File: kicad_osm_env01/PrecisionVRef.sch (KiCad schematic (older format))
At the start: 12 parts

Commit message: schematics awaiting review
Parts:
- added TP86: Test_Point, TestPoint:TestPoint_THTPad_D1.0mm_Drill0.5mm, symbol OSM_env01-rescue:Test_Point-Connector-ESP32-EVB_Rev_D-rescue
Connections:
- net 3V3_AN: now also TP86.1
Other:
- moved on the sheet: C63, C64, C65, L3
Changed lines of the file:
@@
 AR Path="/608F4675/61105411/611114A1" Ref="TP?"  Part="1"
 AR Path="/61323885/611114A1" Ref="TP58"  Part="1"
-F 0 "TP58" V 6320 3797 50  0000 C CNN
-F 1 "Test_Point" V 6229 3797 50  0000 C CNN
+F 0 "TP58" V 6125 4000 50  0000 C CNN
+F 1 "Test_Point" V 6229 3797 50  0001 C CNN
 F 2 "" H 6325 3725 50  0001 C CNN
 F 3 "~" H 6325 3725 50  0001 C CNN
@@
 L power:+5V #PWR?
 U 1 1 611114A7
-P 3275 3525
+P 2725 3550
 AR Path="/608F4675/60959880/611114A7" Ref="#PWR?"  Part="1"
 AR Path="/608F4675/61105411/611114A7" Ref="#PWR?"  Part="1"
 AR Path="/61323885/611114A7" Ref="#PWR0124"  Part="1"
-F 0 "#PWR0124" H 3275 3375 50  0001 C CNN
-F 1 "+5V" H 3290 3698 50  0000 C CNN
-F 2 "" H 3275 3525 50  0001 C CNN
-F 3 "" H 3275 3525 50  0001 C CNN
-	1    3275 3525
+F 0 "#PWR0124" H 2725 3400 50  0001 C CNN
+F 1 "+5V" H 2740 3723 50  0000 C CNN
+F 2 "" H 2725 3550 50  0001 C CNN
+F 3 "" H 2725 3550 50  0001 C CNN
+	1    2725 3550
 	1    0    0    -1
 $EndComp
@@
 L device:Ferrite_Bead L?
 U 1 1 611114BF
-P 3700 3800
+P 3150 3825
 AR Path="/608F4675/60959880/611114BF" Ref="L?"  Part="1"
 AR Path="/608F4675/61105411/611114BF" Ref="L?"  Part="1"
 AR Path="/61323885/611114BF" Ref="L3"  Part="1"
-F 0 "L3" V 3426 3800 50  0000 C CNN
-F 1 "Ferrite_Bead" V 3517 3800 50  0000 C CNN
-F 2 "" V 3630 3800 50  0001 C CNN
-F 3 "" H 3700 3800 50  0001 C CNN
-	1    3700 3800
+F 0 "L3" V 2876 3825 50  0000 C CNN
+F 1 "Ferrite_Bead" V 2967 3825 50  0000 C CNN
+F 2 "" V 3080 3825 50  0001 C CNN
+F 3 "" H 3150 3825 50  0001 C CNN
+	1    3150 3825
 	0    -1   1    0
 $EndComp
@@
 L device:C C?
 U 1 1 611114C5
-P 4650 3950
+P 4100 3975
 AR Path="/608F4675/60959880/611114C5" Ref="C?"  Part="1"
 AR Path="/608F4675/61105411/611114C5" Ref="C?"  Part="1"
 AR Path="/61323885/611114C5" Ref="C64"  Part="1"
-F 0 "C64" H 4765 3996 50  0000 L CNN
-F 1 "10nF" H 4765 3905 50  0000 L CNN
-F 2 "" H 4688 3800 50  0001 C CNN
-F 3 "" H 4650 3950 50  0001 C CNN
-	1    4650 3950
-	-1   0    0    -1
-$EndComp
-Wire Wire Line
-	3550 3800 3275 3800
-Wire Wire Line
-	3275 3525 3275 3800
-Wire Wire Line
-	5125 4200 5125 4100
-Text Label 5450 3800 2    50   ~ 0
+F 0 "C64" H 4215 4021 50  0000 L CNN
+F 1 "10nF" H 4215 3930 50  0000 L CNN
+F 2 "" H 4138 3825 50  0001 C CNN
+F 3 "" H 4100 3975 50  0001 C CNN
+	1    4100 3975
+	-1   0    0    -1
+$EndComp
+Wire Wire Line
+	3000 3825 2725 3825
+Wire Wire Line
+	2725 3550 2725 3825
+Wire Wire Line
+	4575 4225 4575 4125
+Text Label 4900 3825 2    50   ~ 0
 5V_AN
 Wire Wire Line
@@
 $EndComp
 Wire Wire Line
-	8600 3725 8925 3725
+	8600 3725 8750 3725
 Wire Wire Line
 	6625 3725 6975 3725
@@
 Wire Wire Line
 	7275 3725 7675 3725
-Text HLabel 5450 3800 2    50   Input ~ 0
+Text HLabel 4900 3825 2    50   Input ~ 0
 5V_AN
 Text HLabel 8925 3725 2    50   Input ~ 0
@@
 L device:C C?
 U 1 1 61203E74
-P 5125 3950
+P 4575 3975
 AR Path="/608F4675/60959880/61203E74" Ref="C?"  Part="1"
 AR Path="/608F4675/61105411/61203E74" Ref="C?"  Part="1"
 AR Path="/61323885/61203E74" Ref="C65"  Part="1"
-F 0 "C65" H 5240 3996 50  0000 L CNN
-F 1 "100nF" H 5240 3905 50  0000 L CNN
-F 2 "" H 5163 3800 50  0001 C CNN
-F 3 "" H 5125 3950 50  0001 C CNN
-	1    5125 3950
+F 0 "C65" H 4690 4021 50  0000 L CNN
+F 1 "100nF" H 4690 3930 50  0000 L CNN
+F 2 "" H 4613 3825 50  0001 C CNN
+F 3 "" H 4575 3975 50  0001 C CNN
+	1    4575 3975
 	-1   0    0    -1
 $EndComp
@@
 L device:C C?
 U 1 1 61207EE6
-P 4200 3950
+P 3650 3975
 AR Path="/608F4675/60959880/61207EE6" Ref="C?"  Part="1"
 AR Path="/608F4675/61105411/61207EE6" Ref="C?"  Part="1"
 AR Path="/61323885/61207EE6" Ref="C63"  Part="1"
-F 0 "C63" H 4315 3996 50  0000 L CNN
-F 1 "10uF" H 4315 3905 50  0000 L CNN
-F 2 "" H 4238 3800 50  0001 C CNN
-F 3 "" H 4200 3950 50  0001 C CNN
-	1    4200 3950
-	-1   0    0    -1
-$EndComp
-Wire Wire Line
-	3850 3800 4200 3800
-Connection ~ 4200 3800
-Wire Wire Line
-	4200 3800 4650 3800
-Connection ~ 4650 3800
-Wire Wire Line
-	4650 3800 5125 3800
-Connection ~ 5125 3800
-Wire Wire Line
-	5125 3800 5450 3800
-Wire Wire Line
-	4200 4100 4650 4100
-Wire Wire Line
-	4650 4100 5125 4100
-Connection ~ 4650 4100
-Connection ~ 5125 4100
+F 0 "C63" H 3765 4021 50  0000 L CNN
+F 1 "10uF" H 3765 3930 50  0000 L CNN
+F 2 "" H 3688 3825 50  0001 C CNN
+F 3 "" H 3650 3975 50  0001 C CNN
+	1    3650 3975
+	-1   0    0    -1
+$EndComp
+Wire Wire Line
+	3300 3825 3650 3825
+Connection ~ 3650 3825
+Wire Wire Line
+	3650 3825 4100 3825
+Connection ~ 4100 3825
+Wire Wire Line
+	4100 3825 4575 3825
+Connection ~ 4575 3825
+Wire Wire Line
+	4575 3825 4900 3825
+Wire Wire Line
+	3650 4125 4100 4125
+Wire Wire Line
+	4100 4125 4575 4125
+Connection ~ 4100 4125
+Connection ~ 4575 4125
 $Comp
 L device:C C?
@@
 L power:GNDA #PWR?
 U 1 1 6121813D
-P 5125 4200
+P 4575 4225
 AR Path="/608F4675/61105411/6121813D" Ref="#PWR?"  Part="1"
 AR Path="/61323885/6121813D" Ref="#PWR0125"  Part="1"
-F 0 "#PWR0125" H 5125 3950 50  0001 C CNN
-F 1 "GNDA" H 5130 4027 50  0000 C CNN
-F 2 "" H 5125 4200 50  0001 C CNN
-F 3 "" H 5125 4200 50  0001 C CNN
-	1    5125 4200
+F 0 "#PWR0125" H 4575 3975 50  0001 C CNN
+F 1 "GNDA" H 4580 4052 50  0000 C CNN
+F 2 "" H 4575 4225 50  0001 C CNN
+F 3 "" H 4575 4225 50  0001 C CNN
+	1    4575 4225
 	1    0    0    -1
 $EndComp
@@
 $EndComp
 Connection ~ 6625 4175
+$Comp
+L OSM_env01-rescue:Test_Point-Connector-ESP32-EVB_Rev_D-rescue TP?
+U 1 1 6083B3A9
+P 8825 3600
+AR Path="/60688D25/6083B3A9" Ref="TP?"  Part="1"
+AR Path="/61323885/6083B3A9" Ref="TP86"  Part="1"
+F 0 "TP86" V 8825 3875 50  0000 C CNN
+F 1 "Test_Point" V 8929 3672 50  0001 C CNN
+F 2 "TestPoint:TestPoint_THTPad_D1.0mm_Drill0.5mm" H 9025 3600 50  0001 C CNN
+F 3 "~" H 9025 3600 50  0001 C CNN
+	1    8825 3600
+	0    1    1    0
+$EndComp
+Wire Wire Line
+	8825 3600 8750 3600
+Wire Wire Line
+	8750 3600 8750 3725
+Connection ~ 8750 3725
+Wire Wire Line
+	8750 3725 8925 3725
 $EndSCHEMATC

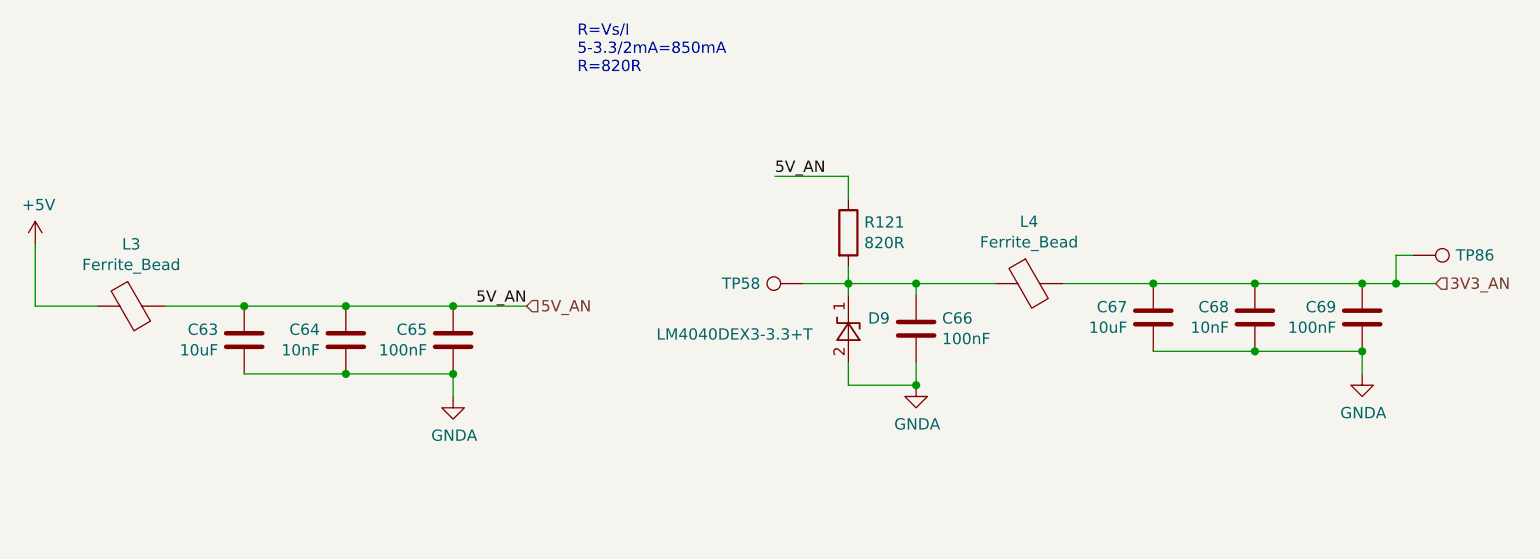
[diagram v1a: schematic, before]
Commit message: updated schematics
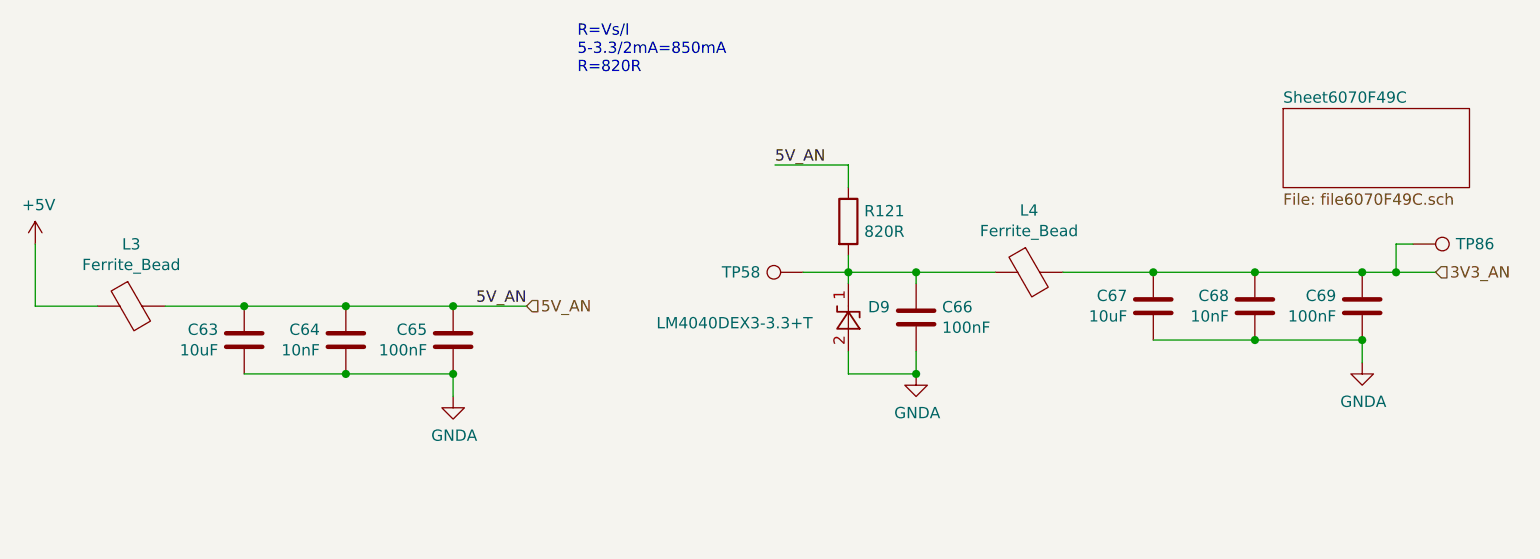
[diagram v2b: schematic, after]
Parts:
- C63, C67: footprint (none) -> Capacitor_SMD:C_0805_2012Metric
- C64, C65, C66, C68, C69: footprint (none) -> Capacitor_SMD:C_0603_1608Metric
- L3, L4: footprint (none) -> Inductor_SMD:L_0805_2012Metric
- R121: footprint (none) -> Resistor_SMD:R_0603_1608Metric
- TP58: footprint (none) -> TestPoint:TestPoint_THTPad_D1.0mm_Drill0.5mm
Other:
- moved on the sheet: C66, C67, C68, C69, D9, L4, R121, TP58, TP86

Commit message: started layout
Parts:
- added TP89: Test_Point, TestPoint:TestPoint_THTPad_D1.0mm_Drill0.5mm, symbol OSM_env01-rescue:Test_Point-Connector-ESP32-EVB_Rev_D-rescue
- D9: footprint TO_SOT_Packages_SMD:SOT-23 -> Devtank_PCB_lib:SC-70-3_package
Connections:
- net 5V_AN: now also TP89.1
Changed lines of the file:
@@
 $Descr A4 11693 8268
 encoding utf-8
-Sheet 11 12
+Sheet 11 11
 Title ""
 Date ""
@@
 Wire Wire Line
 	4575 4225 4575 4125
-Text Label 4900 3825 2    50   ~ 0
+Text Label 4500 3825 2    50   ~ 0
 5V_AN
 Wire Wire Line
@@
 	4100 3825 4575 3825
 Connection ~ 4575 3825
-Wire Wire Line
-	4575 3825 4900 3825
 Wire Wire Line
 	3650 4125 4100 4125
@@
 Wire Wire Line
 	8750 3675 8925 3675
-$Sheet
-S 8250 2950 825  350
-U 6070F49D
-F0 "Sheet6070F49C" 50
-F1 "file6070F49C.sch" 50
-$EndSheet
 $Comp
 L power:GNDA #PWR?
@@
 F 0 "D9" V 6371 3788 50  0000 R CNN
 F 1 "LM4040DEX3-3.3+T" V 6300 4725 50  0000 R CNN
-F 2 "TO_SOT_Packages_SMD:SOT-23" H 6325 3675 50  0001 C CIN
+F 2 "Devtank_PCB_lib:SC-70-3_package" H 6325 3675 50  0001 C CIN
 F 3 "http://www.ti.com/lit/ds/symlink/lm4040-n.pdf" H 6325 3875 50  0001 C CIN
 	1    6325 3875
 	0    -1   -1   0
 $EndComp
+$Comp
+L OSM_env01-rescue:Test_Point-Connector-ESP32-EVB_Rev_D-rescue TP?
+U 1 1 60B8CF4B
+P 4800 3700
+AR Path="/60688D25/60B8CF4B" Ref="TP?"  Part="1"
+AR Path="/61323885/60B8CF4B" Ref="TP89"  Part="1"
+F 0 "TP89" V 4800 3975 50  0000 C CNN
+F 1 "Test_Point" V 4904 3772 50  0001 C CNN
+F 2 "TestPoint:TestPoint_THTPad_D1.0mm_Drill0.5mm" H 5000 3700 50  0001 C CNN
+F 3 "~" H 5000 3700 50  0001 C CNN
+	1    4800 3700
+	0    1    1    0
+$EndComp
+Wire Wire Line
+	4800 3700 4725 3700
+Wire Wire Line
+	4725 3700 4725 3825
+Connection ~ 4725 3825
+Wire Wire Line
+	4725 3825 4900 3825
+Wire Wire Line
+	4575 3825 4725 3825
 $EndSCHEMATC

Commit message: schematics awaiting review
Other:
- note added: "3V3A Ref\n\n"
- note added: "5VA Ref\n\n"
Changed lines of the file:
@@
 $Descr A4 11693 8268
 encoding utf-8
-Sheet 11 11
+Sheet 10 11
 Title ""
 Date ""
@@
 Text HLabel 8925 3675 2    50   Input ~ 0
 3V3_AN
-Text Notes 5125 2800 0    50   ~ 0
+Text Notes 6250 4850 0    50   ~ 0
 R=Vs/I\n5-3.3/2mA=850mA\nR=820R
 $Comp
@@
 Wire Wire Line
 	4575 3825 4725 3825
+Text Notes 3575 3225 0    118  ~ 24
+5VA Ref\n\n
+Text Notes 7175 3200 0    118  ~ 24
+3V3A Ref\n\n
 $EndSCHEMATC

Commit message: rough layout with throwdown of parts
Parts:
- C65, C66, C69: footprint Capacitor_SMD:C_0603_1608Metric -> Capacitor_SMD:C_0402_1005Metric
- D9: footprint Devtank_PCB_lib:SC-70-3_package -> Devtank_PCB_lib:SC-70-3
- TP58, TP86, TP89: footprint TestPoint:TestPoint_THTPad_D1.0mm_Drill0.5mm -> TestPoint:TestPoint_Pad_D1.5mm
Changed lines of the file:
@@
 $Descr A4 11693 8268
 encoding utf-8
-Sheet 10 11
+Sheet 9 10
 Title ""
 Date ""
@@
 F 0 "C65" H 4690 4021 50  0000 L CNN
 F 1 "100nF" H 4690 3930 50  0000 L CNN
-F 2 "Capacitor_SMD:C_0603_1608Metric" H 4613 3825 50  0001 C CNN
+F 2 "Capacitor_SMD:C_0402_1005Metric" H 4613 3825 50  0001 C CNN
 F 3 "" H 4575 3975 50  0001 C CNN
 	1    4575 3975
@@
 F 0 "C69" H 8715 3871 50  0000 L CNN
 F 1 "100nF" H 8715 3780 50  0000 L CNN
-F 2 "Capacitor_SMD:C_0603_1608Metric" H 8638 3675 50  0001 C CNN
+F 2 "Capacitor_SMD:C_0402_1005Metric" H 8638 3675 50  0001 C CNN
 F 3 "" H 8600 3825 50  0001 C CNN
 	1    8600 3825
@@
 F 0 "TP86" V 8825 3825 50  0000 C CNN
 F 1 "Test_Point" V 8929 3622 50  0001 C CNN
-F 2 "TestPoint:TestPoint_THTPad_D1.0mm_Drill0.5mm" H 9025 3550 50  0001 C CNN
+F 2 "TestPoint:TestPoint_Pad_D1.5mm" H 9025 3550 50  0001 C CNN
 F 3 "~" H 9025 3550 50  0001 C CNN
 	1    8825 3550
@@
 F 0 "TP58" V 6125 3950 50  0000 C CNN
 F 1 "Test_Point" V 6229 3747 50  0001 C CNN
-F 2 "TestPoint:TestPoint_THTPad_D1.0mm_Drill0.5mm" H 6325 3675 50  0001 C CNN
+F 2 "TestPoint:TestPoint_Pad_D1.5mm" H 6325 3675 50  0001 C CNN
 F 3 "~" H 6325 3675 50  0001 C CNN
 	1    6125 3675
@@
 F 0 "C66" H 6740 3921 50  0000 L CNN
 F 1 "100nF" H 6740 3830 50  0000 L CNN
-F 2 "Capacitor_SMD:C_0603_1608Metric" H 6663 3725 50  0001 C CNN
+F 2 "Capacitor_SMD:C_0402_1005Metric" H 6663 3725 50  0001 C CNN
 F 3 "" H 6625 3875 50  0001 C CNN
 	1    6625 3875
@@
 F 0 "D9" V 6371 3788 50  0000 R CNN
 F 1 "LM4040DEX3-3.3+T" V 6300 4725 50  0000 R CNN
-F 2 "Devtank_PCB_lib:SC-70-3_package" H 6325 3675 50  0001 C CIN
+F 2 "Devtank_PCB_lib:SC-70-3" H 6325 3675 50  0001 C CIN
 F 3 "http://www.ti.com/lit/ds/symlink/lm4040-n.pdf" H 6325 3875 50  0001 C CIN
 	1    6325 3875
@@
 F 0 "TP89" V 4800 3975 50  0000 C CNN
 F 1 "Test_Point" V 4904 3772 50  0001 C CNN
-F 2 "TestPoint:TestPoint_THTPad_D1.0mm_Drill0.5mm" H 5000 3700 50  0001 C CNN
+F 2 "TestPoint:TestPoint_Pad_D1.5mm" H 5000 3700 50  0001 C CNN
 F 3 "~" H 5000 3700 50  0001 C CNN
 	1    4800 3700
